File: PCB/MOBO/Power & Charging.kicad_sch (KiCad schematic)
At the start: 53 parts, among them J201 MAIN-USBC-OTG/PWR, Q201 AO3401A, Q202 FS8205A, Q203 IRLML6344, Q204 Si4435DDY, SW201 SW_DIP_x01, U201 DW01A, U202 LC709203FQH-01TWG, U203 MCP73871-1AA, U204 TPS61230DRC

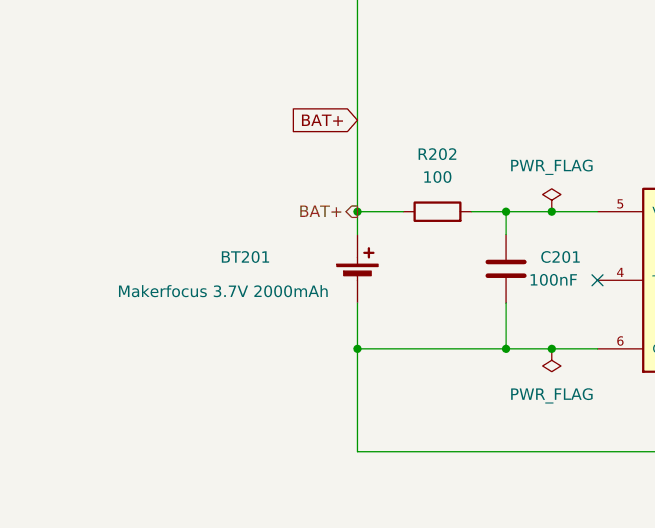
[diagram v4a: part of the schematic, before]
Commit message: fixed battery protection circuit
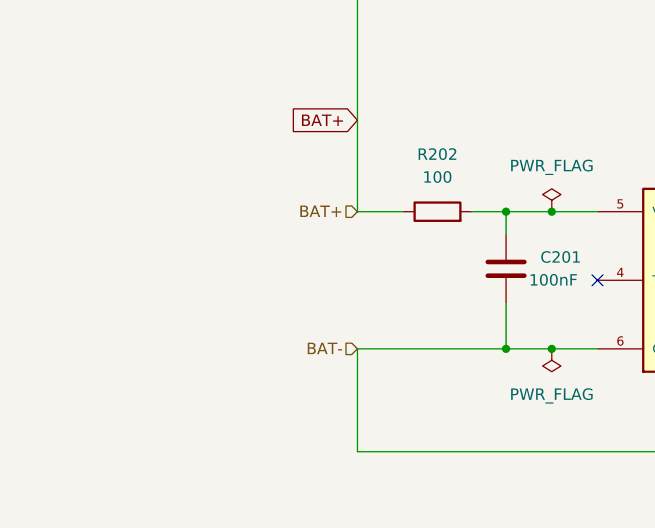
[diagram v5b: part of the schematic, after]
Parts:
- removed BT201: Makerfocus 3.7V 2000mAh, symbol Device:Battery_Cell
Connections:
- net BAT-: now reaches C201.2, Q202.2, Q202.3, U201.6 (GND)
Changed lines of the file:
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@@
   (junction (at 350.52 50.8) (diameter 0) (color 0 0 0 0)
   )
-  (junction (at 53.34 227.33) (diameter 0) (color 0 0 0 0)
-  )
   (junction (at 260.35 78.74) (diameter 0) (color 0 0 0 0)
   )
@@
   )
   (junction (at 257.81 31.75) (diameter 0) (color 0 0 0 0)
-  )
-  (junction (at 53.34 242.57) (diameter 0) (color 0 0 0 0)
   )
   (junction (at 134.62 96.52) (diameter 0) (color 0 0 0 0)
@@
     (stroke (width 0) (type default))
   )
-  (wire (pts (xy 53.34 237.49) (xy 53.34 242.57))
-    (stroke (width 0) (type default))
-  )
   (wire (pts (xy 62.23 36.83) (xy 69.85 36.83))
     (stroke (width 0) (type default))
@@
   )
   (wire (pts (xy 82.55 36.83) (xy 92.71 36.83))
-    (stroke (width 0) (type default))
-  )
-  (wire (pts (xy 53.34 227.33) (xy 53.34 229.87))
     (stroke (width 0) (type default))
   )
@@
     (effects (font (size 1.27 1.27)) (justify right))
   )
-  (hierarchical_label "BAT+" (shape output) (at 53.34 227.33 180) (fields_autoplaced)
+  (hierarchical_label "BAT+" (shape input) (at 53.34 227.33 180) (fields_autoplaced)
+    (effects (font (size 1.27 1.27)) (justify right))
+  )
+  (hierarchical_label "BAT-" (shape input) (at 53.34 242.57 180) (fields_autoplaced)
     (effects (font (size 1.27 1.27)) (justify right))
   )
@@
         )
       )
-    )
-  )
-  (symbol (lib_id "Device:Battery_Cell") (at 53.34 234.95 0) (unit 1)
-    (in_bom yes) (on_board yes) (dnp no)
-    (property "Reference" "BT201" (at 38.1 232.41 0)
-      (effects (font (size 1.27 1.27)) (justify left))
-    )
-    (property "Value" "Makerfocus 3.7V 2000mAh" (at 26.67 236.22 0)
-      (effects (font (size 1.27 1.27)) (justify left))
-    )
-    (property "Footprint" "" (at 53.34 233.426 90)
-      (effects (font (size 1.27 1.27)) hide)
-    )
-    (property "Datasheet" "~" (at 53.34 233.426 90)
-      (effects (font (size 1.27 1.27)) hide)
-    )
-    (pin "1")
-    (pin "2")
-    (instances
-      (project "MOBO"
-        (path "/2d62a3c1-c4f2-4921-9f6b-8dc8aef69d64/968b581c-59b8-4e39-ae9d-82f589704db7"
-          (reference "BT201") (unit 1)
-        )
-      )

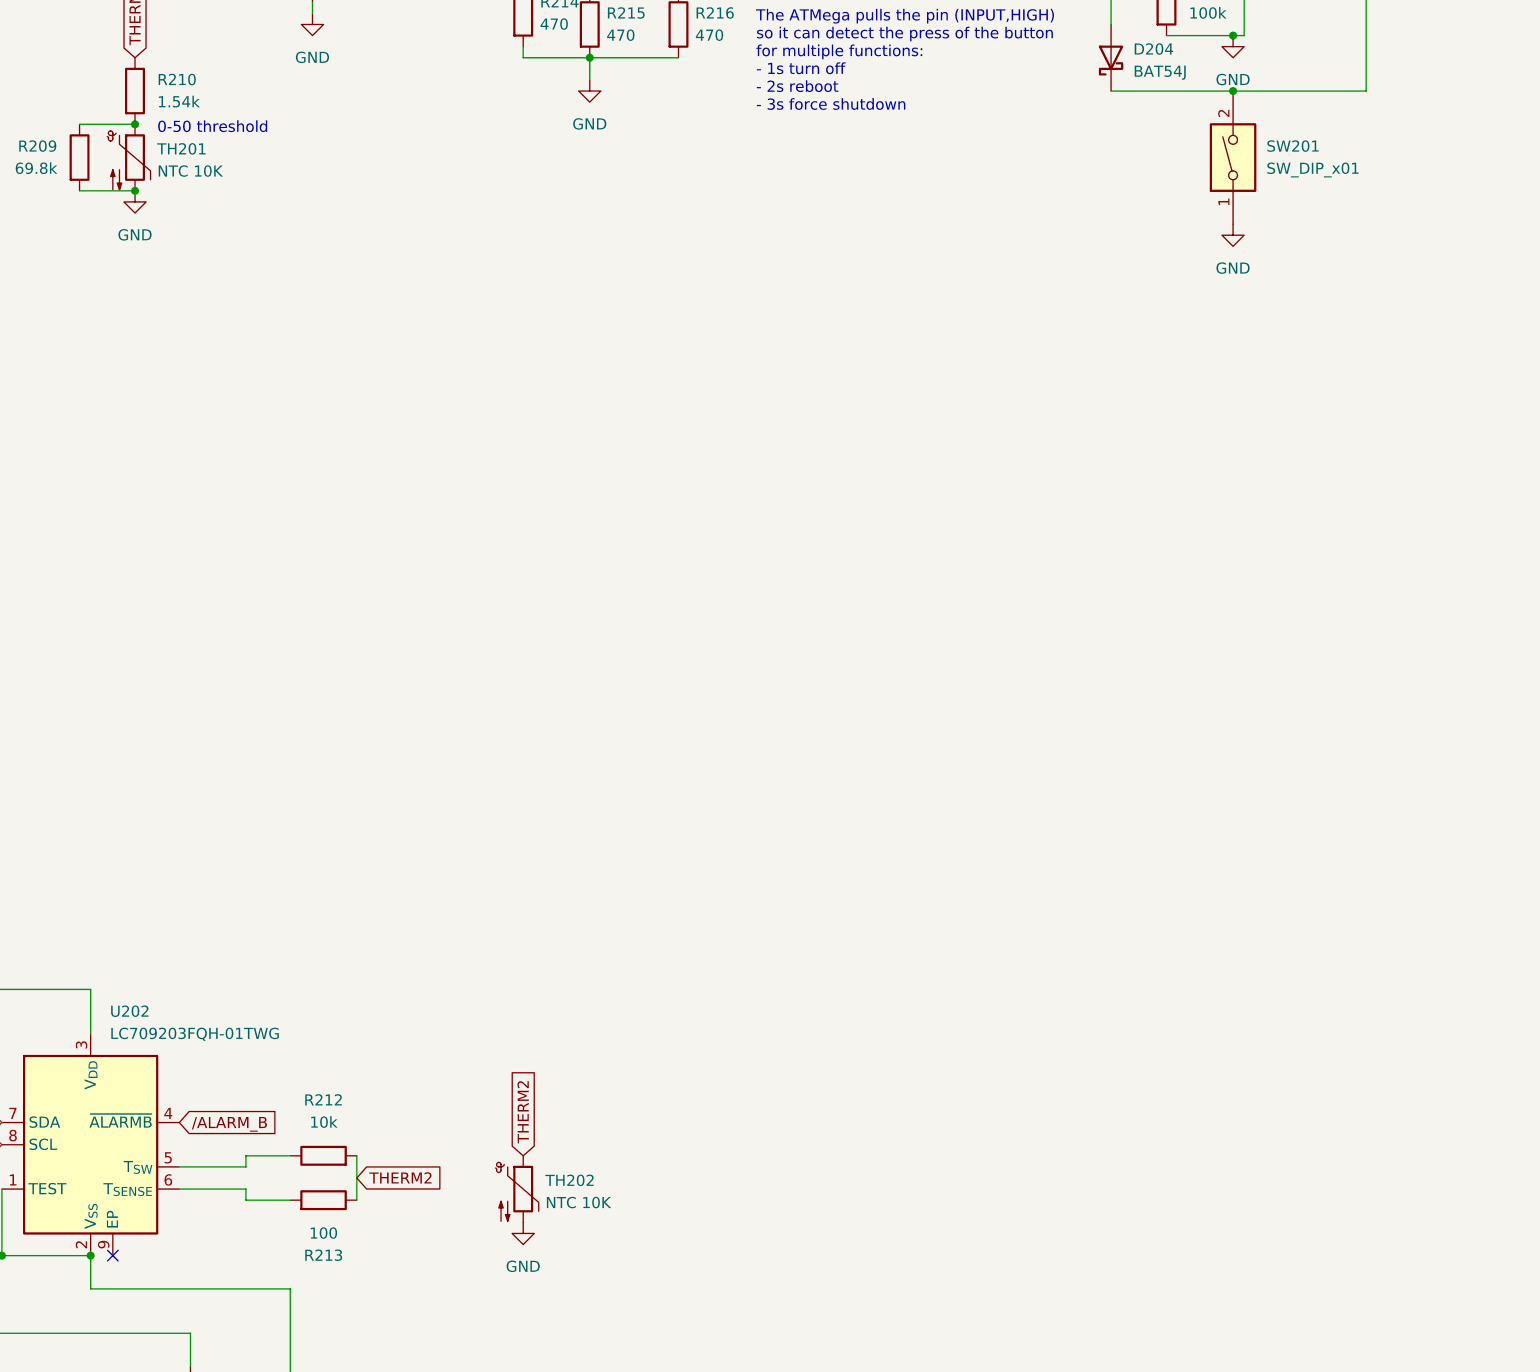
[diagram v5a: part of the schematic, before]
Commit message: added all footprints
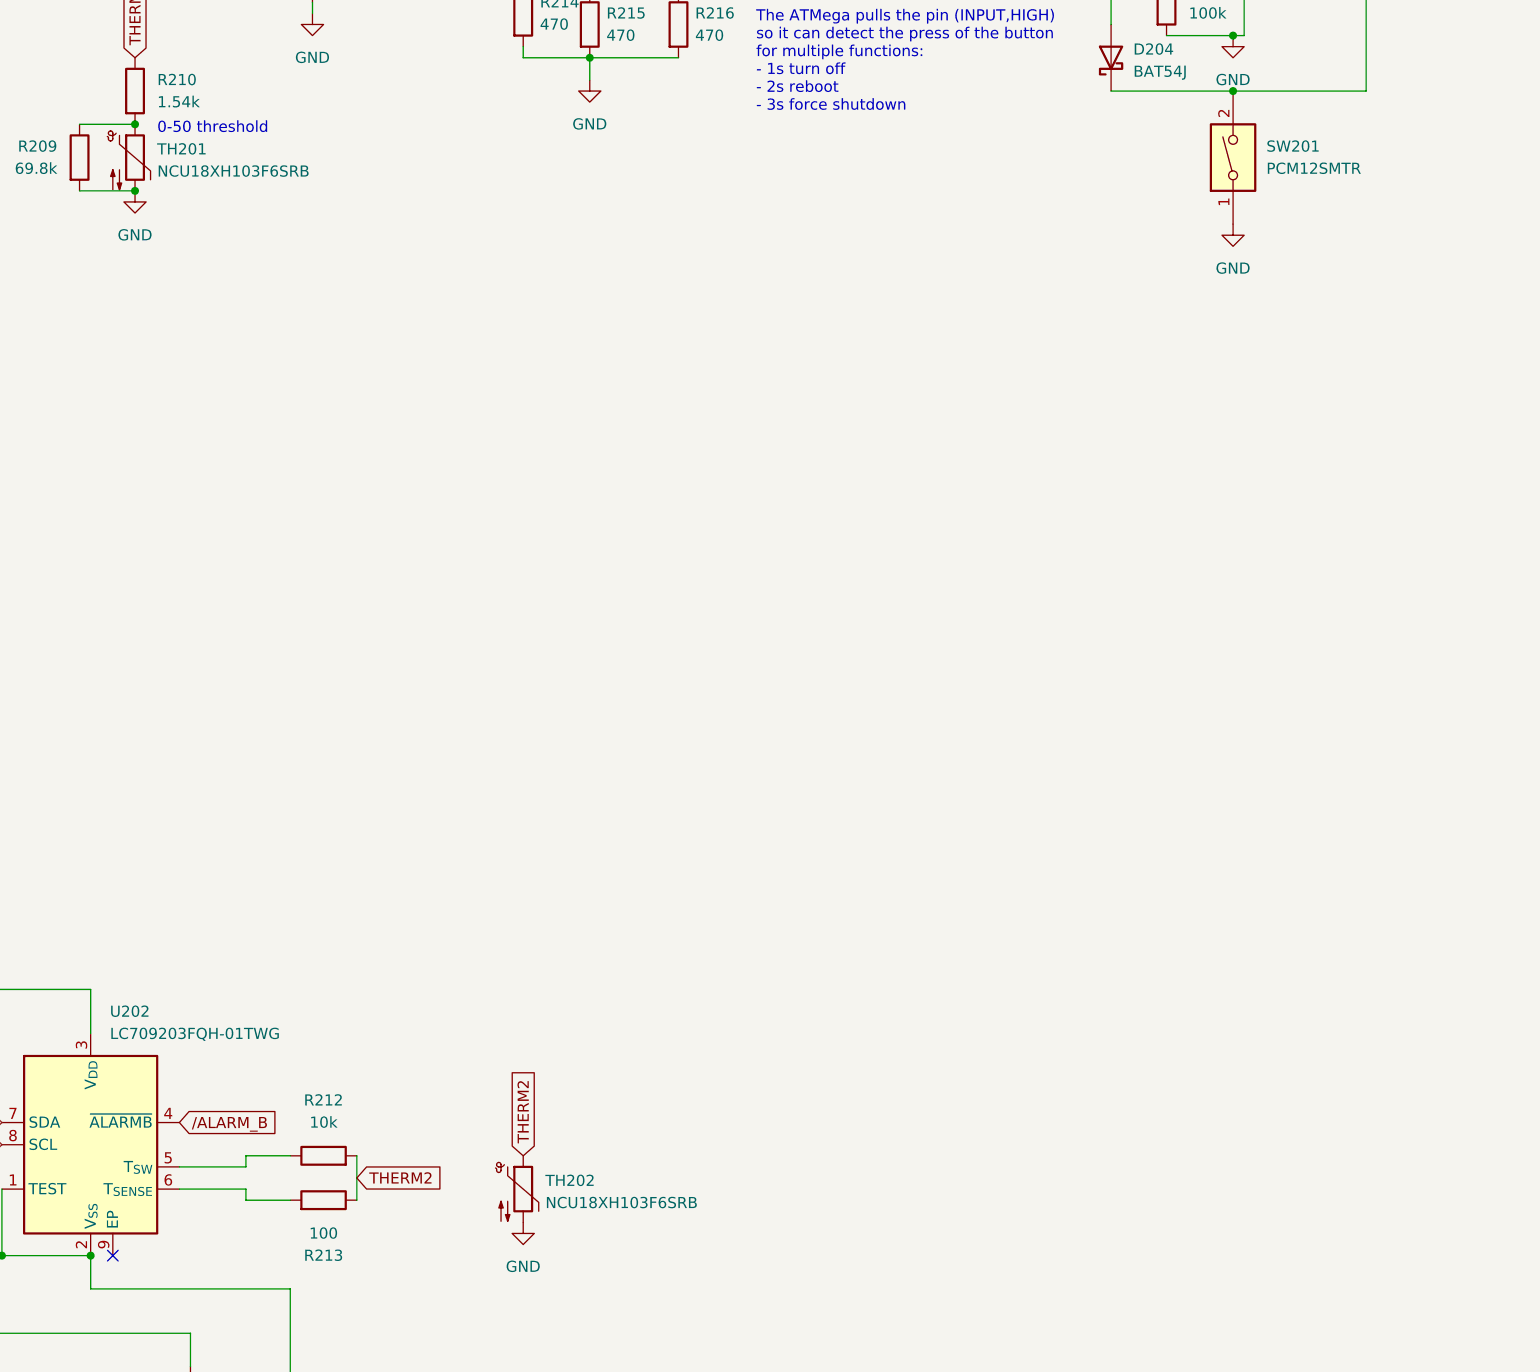
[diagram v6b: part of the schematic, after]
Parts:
- C201, C202, C203, C204, C205, C206, C207, C208, C209, C210, C211: footprint (none) -> Capacitor_SMD:C_0805_2012Metric
- D201, D202, D203: footprint (none) -> LED_SMD:LED_0805_2012Metric
- F201: footprint (none) -> Fuse:Fuse_0805_2012Metric
- J201: footprint (none) -> Connector_USB:USB_C_Receptacle_GCT_USB4085
- L201: footprint (none) -> Inductor_SMD:L_0805_2012Metric
- Q203: footprint Package_TO_SOT_SMD_AKL:SOT-23 -> Package_TO_SOT_SMD:SOT-23
- Q204: footprint Package_SO_AKL:SO-8_3.9x4.9mm_P1.27mm -> Package_SO:SOIC-8-1EP_3.9x4.9mm_P1.27mm_EP2.41x3.3mm
- R201, R202, R203, R204, R205, R206, R207, R208, R209, R210, R211, R212, R213, R214, R215, R216, R217, R218, R219, R220, R221, R222: footprint (none) -> Resistor_SMD:R_0805_2012Metric
- SW201: value SW_DIP_x01 -> PCM12SMTR; footprint (none) -> Button_Switch_SMD:SW_SPDT_PCM12
- TH201, TH202: value NTC 10K -> NCU18XH103F6SRB; footprint (none) -> Capacitor_SMD:C_0603_1608Metric

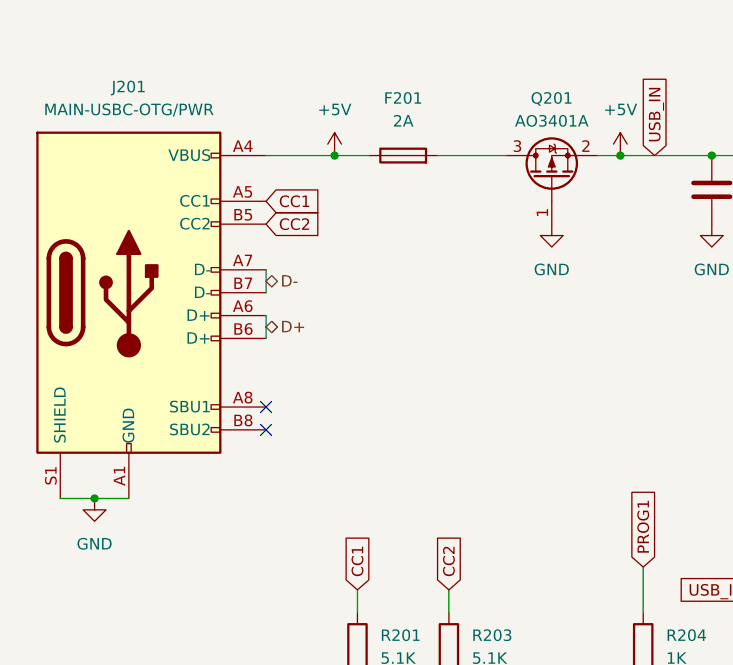
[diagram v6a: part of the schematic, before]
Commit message: added usb esd ic and footprint
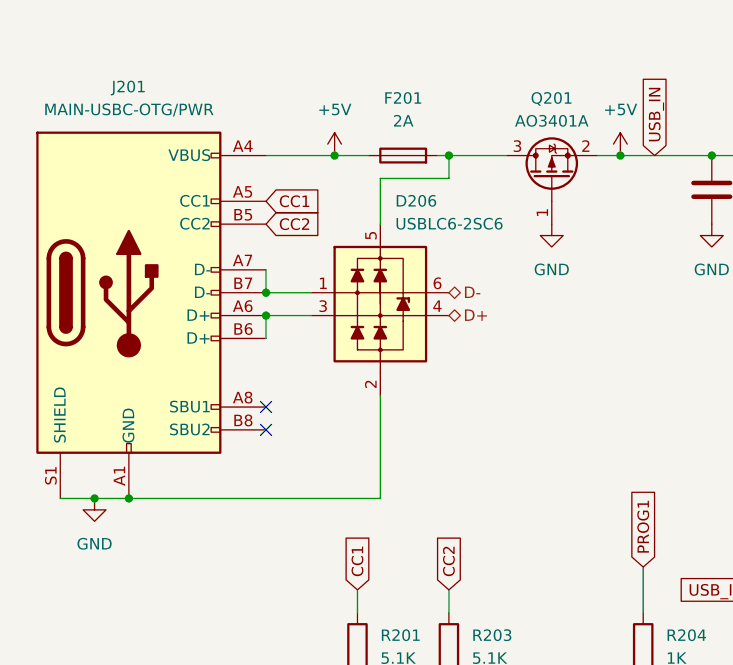
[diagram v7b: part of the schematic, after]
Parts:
- added D206: USBLC6-2SC6, Package_TO_SOT_SMD:SOT-23-6, symbol PCM_Diode_TVS_AKL:USBLC6-2SC6
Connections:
- net D+: now also D206.4 (L2); no longer J201.A6 (D+), J201.B6 (D+)
- net D-: now also D206.6 (L1); no longer J201.A7 (D-), J201.B7 (D-)
- net GND: now also D206.2 (VN)
- net at F201.2, Q201.3 (D): now also D206.5 (VP)
- new net: D206.1 (L1), J201.A7 (D-), J201.B7 (D-)
- new net: D206.3 (L2), J201.A6 (D+), J201.B6 (D+)
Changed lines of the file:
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@@
   (junction (at 257.81 36.83) (diameter 0) (color 0 0 0 0)
   )
+  (junction (at 27.94 74.93) (diameter 0) (color 0 0 0 0)
+  )
   (junction (at 350.52 50.8) (diameter 0) (color 0 0 0 0)
   )
@@
   (junction (at 50.8 36.83) (diameter 0) (color 0 0 0 0)
   )
+  (junction (at 63.5 36.83) (diameter 0) (color 0 0 0 0)
+  )
+  (junction (at 43.18 54.61) (diameter 0) (color 0 0 0 0)
+  )
   (junction (at 350.52 43.18) (diameter 0) (color 0 0 0 0)
   )
@@
   )
   (junction (at 283.21 36.83) (diameter 0) (color 0 0 0 0)
+  )
+  (junction (at 43.18 52.07) (diameter 0) (color 0 0 0 0)
   )
   (junction (at 260.35 85.09) (diameter 0) (color 0 0 0 0)
@@
     (stroke (width 0) (type default))
   )
-  (wire (pts (xy 62.23 36.83) (xy 69.85 36.83))
+  (wire (pts (xy 62.23 36.83) (xy 63.5 36.83))
     (stroke (width 0) (type default))
   )
@@
     (stroke (width 0) (type default))
   )
+  (wire (pts (xy 43.18 54.61) (xy 48.26 54.61))
+    (stroke (width 0) (type default))
+  )
   (wire (pts (xy 139.7 208.28) (xy 147.32 208.28))
     (stroke (width 0) (type default))
@@
     (stroke (width 0) (type default))
   )
+  (wire (pts (xy 43.18 52.07) (xy 48.26 52.07))
+    (stroke (width 0) (type default))
+  )
   (wire (pts (xy 140.97 254) (xy 130.81 254))
     (stroke (width 0) (type default))
@@
     (stroke (width 0) (type default))
   )
+  (wire (pts (xy 55.88 74.93) (xy 55.88 63.5))
+    (stroke (width 0) (type default))
+  )
   (wire (pts (xy 147.32 208.28) (xy 147.32 207.01))
     (stroke (width 0) (type default))
@@
     (stroke (width 0) (type default))
   )
+  (wire (pts (xy 55.88 39.37) (xy 63.5 39.37))
+    (stroke (width 0) (type default))
+  )
+  (wire (pts (xy 63.5 36.83) (xy 69.85 36.83))
+    (stroke (width 0) (type default))
+  )
   (wire (pts (xy 102.87 67.31) (xy 102.87 36.83))
     (stroke (width 0) (type default))
@@
     (stroke (width 0) (type default))
   )
+  (wire (pts (xy 63.5 39.37) (xy 63.5 36.83))
+    (stroke (width 0) (type default))
+  )
   (wire (pts (xy 69.85 242.57) (xy 74.93 242.57))
     (stroke (width 0) (type default))
@@
     (stroke (width 0) (type default))
   )
+  (wire (pts (xy 55.88 39.37) (xy 55.88 44.45))
+    (stroke (width 0) (type default))
+  )
   (wire (pts (xy 66.04 227.33) (xy 69.85 227.33))
     (stroke (width 0) (type default))
@@
   )
   (wire (pts (xy 152.4 222.25) (xy 152.4 254))
+    (stroke (width 0) (type default))
+  )
+  (wire (pts (xy 27.94 74.93) (xy 55.88 74.93))
     (stroke (width 0) (type default))
   )
@@
     (effects (font (size 1.27 1.27)) (justify right))
   )
-  (hierarchical_label "D+" (shape bidirectional) (at 43.18 55.88 0) (fields_autoplaced)
+  (hierarchical_label "D+" (shape bidirectional) (at 63.5 54.61 0) (fields_autoplaced)
     (effects (font (size 1.27 1.27)) (justify left))
   )
@@
     (effects (font (size 1.27 1.27)) (justify left))
   )
-  (hierarchical_label "D-" (shape bidirectional) (at 43.18 50.8 0) (fields_autoplaced)
+  (hierarchical_label "D-" (shape bidirectional) (at 63.5 52.07 0) (fields_autoplaced)
     (effects (font (size 1.27 1.27)) (justify left))
   )
@@
         )
       )
+    )
+  )
+  (symbol (lib_id "PCM_Diode_TVS_AKL:USBLC6-2SC6") (at 55.88 52.07 0) (unit 1)
+    (in_bom yes) (on_board yes) (dnp no) (fields_autoplaced)
+    (property "Reference" "D206" (at 57.5311 41.91 0)
+      (effects (font (size 1.27 1.27)) (justify left))
+    )
+    (property "Value" "USBLC6-2SC6" (at 57.5311 44.45 0)
+      (effects (font (size 1.27 1.27)) (justify left))
+    )
+    (property "Footprint" "Package_TO_SOT_SMD:SOT-23-6" (at 55.88 52.07 0)
+      (effects (font (size 1.27 1.27)) hide)
+    )
+    (property "Datasheet" "https://www.tme.eu/Document/db59d28d28a96c34f26d05f234ff409c/USBLC6-2.pdf" (at 55.88 52.07 0)
+      (effects (font (size 1.27 1.27)) hide)
+    )
+    (pin "5")
+    (pin "6")
+    (pin "4")
+    (pin "3")
+    (pin "2")
+    (pin "1")
+    (instances
+      (project "MOBO"
+        (path "/2d62a3c1-c4f2-4921-9f6b-8dc8aef69d64/968b581c-59b8-4e39-ae9d-82f589704db7"
+          (reference "D206") (unit 1)
+        )
+      )
